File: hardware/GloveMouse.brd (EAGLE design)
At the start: 42 x 40.5 mm, 57 parts, among them IC3 MCP73811/2, J1 USB MICRO, Q1 ABM3B-16, Q2 32.768kHz, U2 LPY403AL, U3 ANTENNA, U4 MCP1825S-3302E/DB, U5 BALUN, U6 ATMEGA128RFA1

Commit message: v3.0 release candidate 2
Changed grounding for ATmega128RFA1 so that it doesn't pass through antenna
ground plane.
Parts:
- moved R8 1.50 mm to (30.0, 8.50)
- moved C13 1.00 mm to (32.5, 7.50)
- moved R7 1.00 mm to (32.5, 9.50)
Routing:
- net GND: track 260.4 -> 263.5 mm
- net BAT: track 125.4 -> 124.4 mm
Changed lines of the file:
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@@
 </element>
 <element name="C11" library="resistor" package="C0603K" value="1uF" x="40" y="7.5" rot="MR270"/>
-<element name="C13" library="resistor" package="C0603K" value="10uF" x="31.5" y="7.5" rot="MR0"/>
+<element name="C13" library="resistor" package="C0603K" value="10uF" x="32.5" y="7.5" rot="MR0"/>
 <element name="R13" library="resistor" package="R0603" value="10K" x="32" y="30.5" rot="MR0"/>
 <element name="PWR_LED" library="led" package="CHIP-LED0805" value="GREEN" x="34.5" y="8.5" rot="R180"/>
@@
 <element name="R9" library="resistor" package="R0603" value="10k" x="28.5" y="8.5" rot="R90"/>
 <element name="R14" library="resistor" package="R0603" value="10k" x="28" y="22.5" rot="R90"/>
-<element name="R7" library="resistor" package="R0603" value="100k" x="31.5" y="9.5" rot="MR0"/>
-<element name="R8" library="resistor" package="R0603" value="100k" x="28.5" y="8.5" rot="MR90"/>
+<element name="R7" library="resistor" package="R0603" value="100k" x="32.5" y="9.5" rot="MR0"/>
+<element name="R8" library="resistor" package="R0603" value="100k" x="30" y="8.5" rot="MR90"/>
 <element name="Q2" library="crystal" package="FC-12M" value="32.768kHz" x="25.5" y="19" rot="MR270"/>
 </elements>
@@
 <wire x1="14.5" y1="6.5" x2="19.85" y2="11.85" width="0.4064" layer="16"/>
 <wire x1="19.85" y1="11.85" x2="19.85" y2="13" width="0.4064" layer="16"/>
-<wire x1="25" y1="8.5" x2="25" y2="11.5" width="0.4064" layer="16"/>
-<wire x1="25" y1="11.5" x2="23.75" y2="12.75" width="0.4064" layer="16"/>
 <wire x1="27.25" y1="18.75" x2="28" y2="19.5" width="0.254" layer="1"/>
 <wire x1="28" y1="19.5" x2="28" y2="21.65" width="0.254" layer="1"/>
@@
 <wire x1="22.75" y1="15.5" x2="22.75" y2="18.25" width="0.254" layer="1"/>
 <wire x1="23.65" y1="17.35" x2="22" y2="19" width="0.4064" layer="16"/>
-<wire x1="23.75" y1="12.75" x2="23.75" y2="16.4" width="0.4064" layer="16"/>
 <wire x1="23.65" y1="17.35" x2="23.65" y2="16.5" width="0.4064" layer="16"/>
 <wire x1="23.65" y1="16.5" x2="23.75" y2="16.4" width="0.4064" layer="16"/>
@@
 <wire x1="4" y1="9" x2="5" y2="9" width="0.4064" layer="1"/>
 <wire x1="3.7554" y1="11.2554" x2="3.5" y2="11" width="0.3048" layer="1"/>
-<wire x1="28.73" y1="4.81" x2="28.5" y2="5.04" width="0.4064" layer="16"/>
-<wire x1="28.5" y1="5.04" x2="28.5" y2="7.65" width="0.4064" layer="16"/>
-<wire x1="28.5" y1="7.65" x2="30.625" y2="7.65" width="0.4064" layer="16"/>
-<wire x1="30.625" y1="7.65" x2="30.625" y2="7.5" width="0.4064" layer="16"/>
 <wire x1="31.5" y1="7.45" x2="28.5" y2="7.45" width="0.4064" layer="1"/>
 <wire x1="28.5" y1="7.45" x2="28.5" y2="7.65" width="0.4064" layer="1"/>
@@
 <wire x1="22.5" y1="5.625" x2="24.125" y2="5.625" width="0.254" layer="1"/>
 <wire x1="24.125" y1="5.625" x2="25" y2="6.5" width="0.254" layer="1"/>
+<wire x1="23.75" y1="16.4" x2="23.75" y2="13.75" width="0.4064" layer="16"/>
+<wire x1="23.75" y1="13.75" x2="28.73" y2="8.77" width="0.4064" layer="16"/>
+<wire x1="28.73" y1="4.81" x2="28.73" y2="7" width="0.4064" layer="16"/>
+<wire x1="28.73" y1="7" x2="28.73" y2="7.23" width="0.4064" layer="16"/>
+<wire x1="28.73" y1="7.23" x2="29.15" y2="7.65" width="0.4064" layer="16"/>
+<wire x1="29.15" y1="7.65" x2="30" y2="7.65" width="0.4064" layer="16"/>
+<wire x1="31.625" y1="7.5" x2="31.475" y2="7.65" width="0.4064" layer="16"/>
+<wire x1="31.475" y1="7.65" x2="30" y2="7.65" width="0.4064" layer="16"/>
+<wire x1="28.73" y1="8.77" x2="28.73" y2="7.23" width="0.4064" layer="16"/>
 </signal>
 <signal name="RESET">
@@
 <wire x1="26.27" y1="29.23" x2="25.04" y2="29.23" width="0.4064" layer="16"/>
 <wire x1="23.75" y1="14.5" x2="23.75" y2="13.25" width="0.254" layer="1"/>
-<via x="27" y="11.5" extent="1-16" drill="0.8" diameter="1.6"/>
+<via x="29" y="12.5" extent="1-16" drill="0.8" diameter="1.6"/>
 <wire x1="31" y1="14" x2="31" y2="21.5" width="0.4064" layer="16"/>
 <wire x1="35.2512" y1="25.7512" x2="35.2512" y2="28.2394" width="0.4064" layer="16"/>
@@
 <wire x1="35.2512" y1="29.2488" x2="34" y2="30.5" width="0.4064" layer="16"/>
 <wire x1="34" y1="30.5" x2="32.85" y2="30.5" width="0.4064" layer="16"/>
-<wire x1="28.5" y1="11.5" x2="31" y2="14" width="0.4064" layer="16"/>
-<wire x1="23.75" y1="13.25" x2="25.5" y2="11.5" width="0.254" layer="1"/>
-<wire x1="25.5" y1="11.5" x2="27" y2="11.5" width="0.254" layer="1"/>
-<wire x1="28.5" y1="11.5" x2="27" y2="11.5" width="0.4064" layer="16"/>
+<wire x1="23.75" y1="13.25" x2="25" y2="12" width="0.254" layer="1"/>
 <wire x1="31" y1="21.5" x2="35.2512" y2="25.7512" width="0.4064" layer="16"/>
+<wire x1="25" y1="12" x2="28.5" y2="12" width="0.254" layer="1"/>
+<wire x1="28.5" y1="12" x2="29" y2="12.5" width="0.254" layer="1"/>
+<wire x1="29" y1="12.5" x2="29.5" y2="12.5" width="0.4064" layer="16"/>
+<wire x1="29.5" y1="12.5" x2="31" y2="14" width="0.4064" layer="16"/>
 </signal>
 <signal name="+3V3">
@@
 <contactref element="R7" pad="1"/>
 <contactref element="LIPO" pad="1"/>
-<wire x1="32.35" y1="9.5" x2="33.5" y2="9.5" width="0.4064" layer="16"/>
-<wire x1="33.5" y1="9.5" x2="34.6886" y2="10.6886" width="0.4064" layer="16"/>
-<wire x1="34.6886" y1="10.6886" x2="34.6886" y2="14.7004" width="0.4064" layer="16"/>
-<wire x1="31.27" y1="4.81" x2="32.375" y2="5.915" width="0.4064" layer="16"/>
-<wire x1="32.375" y1="5.915" x2="32.375" y2="7.5" width="0.4064" layer="16"/>
-<wire x1="32.35" y1="9.5" x2="32.375" y2="9.475" width="0.4064" layer="16"/>
-<wire x1="32.375" y1="9.475" x2="32.375" y2="7.5" width="0.4064" layer="16"/>
+<wire x1="33.35" y1="11.35" x2="34.6886" y2="12.6886" width="0.4064" layer="16"/>
+<wire x1="34.6886" y1="12.6886" x2="34.6886" y2="14.7004" width="0.4064" layer="16"/>
+<wire x1="33.35" y1="9.5" x2="33.375" y2="9.475" width="0.4064" layer="16"/>
+<wire x1="33.375" y1="9.475" x2="33.375" y2="7.5" width="0.4064" layer="16"/>
 <wire x1="35.55" y1="18.7" x2="35.5" y2="18.65" width="0.4064" layer="16"/>
 <wire x1="35.5" y1="18.65" x2="35.5" y2="16.5" width="0.4064" layer="16"/>
 <wire x1="35.5" y1="16.5" x2="34.6886" y2="15.6886" width="0.4064" layer="16"/>
 <wire x1="34.6886" y1="15.6886" x2="34.6886" y2="14.7004" width="0.4064" layer="16"/>
+<wire x1="33.35" y1="11.35" x2="33.35" y2="9.5" width="0.4064" layer="16"/>
+<wire x1="31.27" y1="4.81" x2="32.31" y2="4.81" width="0.4064" layer="16"/>
+<wire x1="32.31" y1="4.81" x2="33.375" y2="5.875" width="0.4064" layer="16"/>
+<wire x1="33.375" y1="5.875" x2="33.375" y2="7.5" width="0.4064" layer="16"/>
 </signal>
 <signal name="LCLICK">
@@
 <wire x1="1.5" y1="6" x2="0.5" y2="7" width="0.4064" layer="1"/>
 <via x="34" y="17.5" extent="1-16" drill="0.8" diameter="1.6"/>
-<wire x1="30.65" y1="10.65" x2="30.65" y2="9.5" width="0.4064" layer="16"/>
+<wire x1="31.65" y1="12.15" x2="31.65" y2="9.5" width="0.4064" layer="16"/>
 <wire x1="0.5" y1="32" x2="8.5" y2="40" width="0.4064" layer="1"/>
 <wire x1="38" y1="34.5" x2="32.5" y2="40" width="0.4064" layer="1"/>
-<wire x1="28.5" y1="9.35" x2="30.65" y2="9.35" width="0.4064" layer="16"/>
-<wire x1="30.65" y1="9.35" x2="30.65" y2="9.5" width="0.4064" layer="16"/>
-<wire x1="30.65" y1="10.65" x2="32.5" y2="12.5" width="0.4064" layer="16"/>
-<wire x1="32.5" y1="12.5" x2="32.5" y2="16" width="0.4064" layer="16"/>
+<wire x1="31.65" y1="12.15" x2="32.5" y2="13" width="0.4064" layer="16"/>
+<wire x1="32.5" y1="13" x2="32.5" y2="16" width="0.4064" layer="16"/>
 <wire x1="32.5" y1="16" x2="34" y2="17.5" width="0.4064" layer="16"/>
 <wire x1="34" y1="24.5" x2="35" y2="25.5" width="0.4064" layer="1"/>
 <wire x1="35" y1="25.5" x2="37" y2="25.5" width="0.4064" layer="1"/>
 <wire x1="37" y1="25.5" x2="38" y2="26.5" width="0.4064" layer="1"/>
+<wire x1="31.65" y1="9.5" x2="31.5" y2="9.35" width="0.4064" layer="16"/>
+<wire x1="31.5" y1="9.35" x2="30" y2="9.35" width="0.4064" layer="16"/>
 </signal>
 <signal name="N$23">

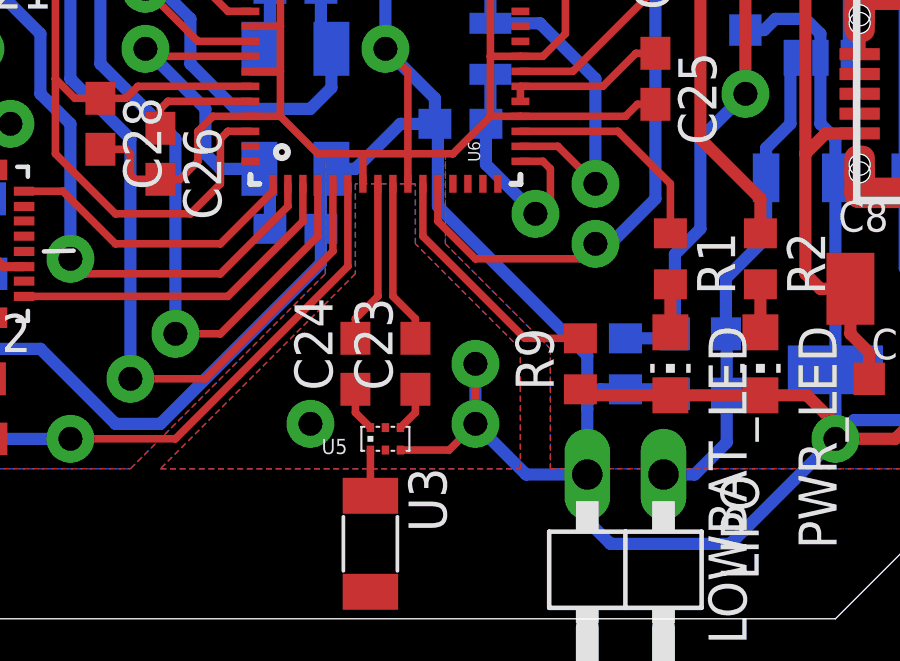
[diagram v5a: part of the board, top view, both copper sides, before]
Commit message: v3.0 release candidate 3
Changed grounding for antenna.
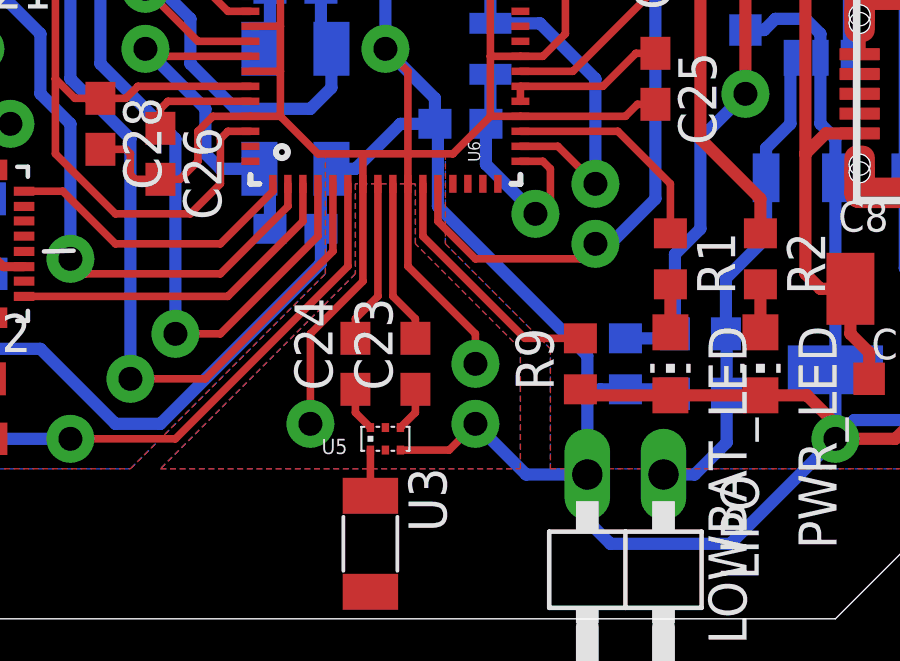
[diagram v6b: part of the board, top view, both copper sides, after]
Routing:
- net GND: track 263.5 -> 275.2 mm
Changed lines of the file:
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@@
 <contactref element="LIPO" pad="2"/>
 <via x="25" y="8.5" extent="1-16" drill="0.8" diameter="1.6"/>
-<wire x1="25" y1="8.5" x2="25" y2="6.5" width="0.4064" layer="16"/>
 <wire x1="25" y1="6.5" x2="26.69" y2="4.81" width="0.4064" layer="16"/>
 <wire x1="26.69" y1="4.81" x2="28.73" y2="4.81" width="0.4064" layer="16"/>
-<wire x1="25" y1="6.5" x2="25" y2="8.5" width="0.254" layer="1"/>
 <wire x1="5.45" y1="24.5" x2="5.45" y2="22.5" width="0.4064" layer="1"/>
 <via x="5" y="28" extent="1-16" drill="0.8" diameter="1.6"/>
@@
 <wire x1="23.75" y1="16.4" x2="23.75" y2="13.75" width="0.4064" layer="16"/>
 <wire x1="23.75" y1="13.75" x2="28.73" y2="8.77" width="0.4064" layer="16"/>
-<wire x1="28.73" y1="4.81" x2="28.73" y2="7" width="0.4064" layer="16"/>
-<wire x1="28.73" y1="7" x2="28.73" y2="7.23" width="0.4064" layer="16"/>
+<wire x1="28.73" y1="4.81" x2="28.73" y2="7.23" width="0.4064" layer="16"/>
 <wire x1="28.73" y1="7.23" x2="29.15" y2="7.65" width="0.4064" layer="16"/>
 <wire x1="29.15" y1="7.65" x2="30" y2="7.65" width="0.4064" layer="16"/>
@@
 <wire x1="31.475" y1="7.65" x2="30" y2="7.65" width="0.4064" layer="16"/>
 <wire x1="28.73" y1="8.77" x2="28.73" y2="7.23" width="0.4064" layer="16"/>
+<wire x1="25" y1="8.5" x2="25" y2="9.5" width="0.254" layer="1"/>
+<wire x1="19.5" y1="6.5" x2="19.5" y2="9.5" width="0.254" layer="1"/>
+<wire x1="19.5" y1="9.5" x2="21.25" y2="11.25" width="0.254" layer="1"/>
+<wire x1="21.25" y1="11.25" x2="21.25" y2="14.5" width="0.254" layer="1"/>
+<wire x1="25" y1="9.5" x2="22.75" y2="11.75" width="0.254" layer="1"/>
+<wire x1="22.75" y1="11.75" x2="22.75" y2="14.5" width="0.254" layer="1"/>
 </signal>
 <signal name="RESET">
